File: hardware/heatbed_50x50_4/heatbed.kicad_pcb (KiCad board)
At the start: 2 copper layers, 50 x 50 mm, 1 part, among them J1 PWR

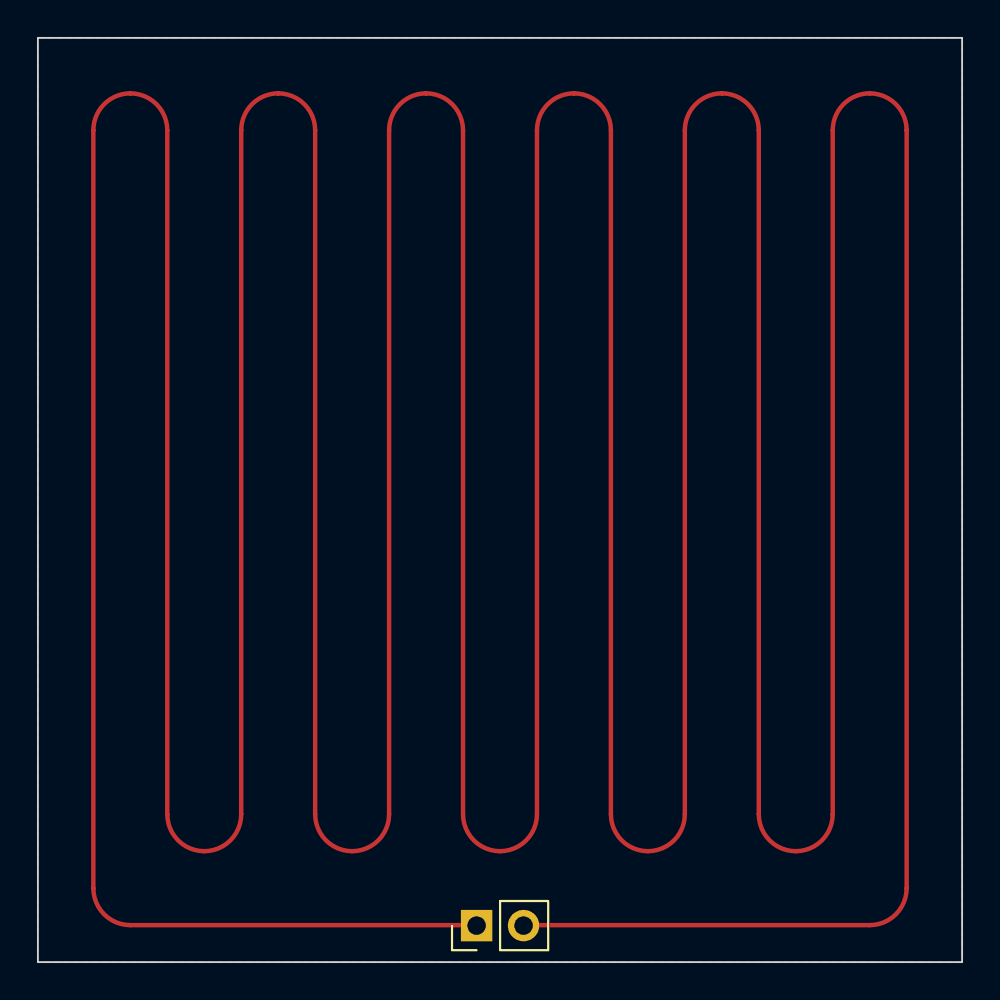
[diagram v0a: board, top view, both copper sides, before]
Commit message: Further increase tracks' widths
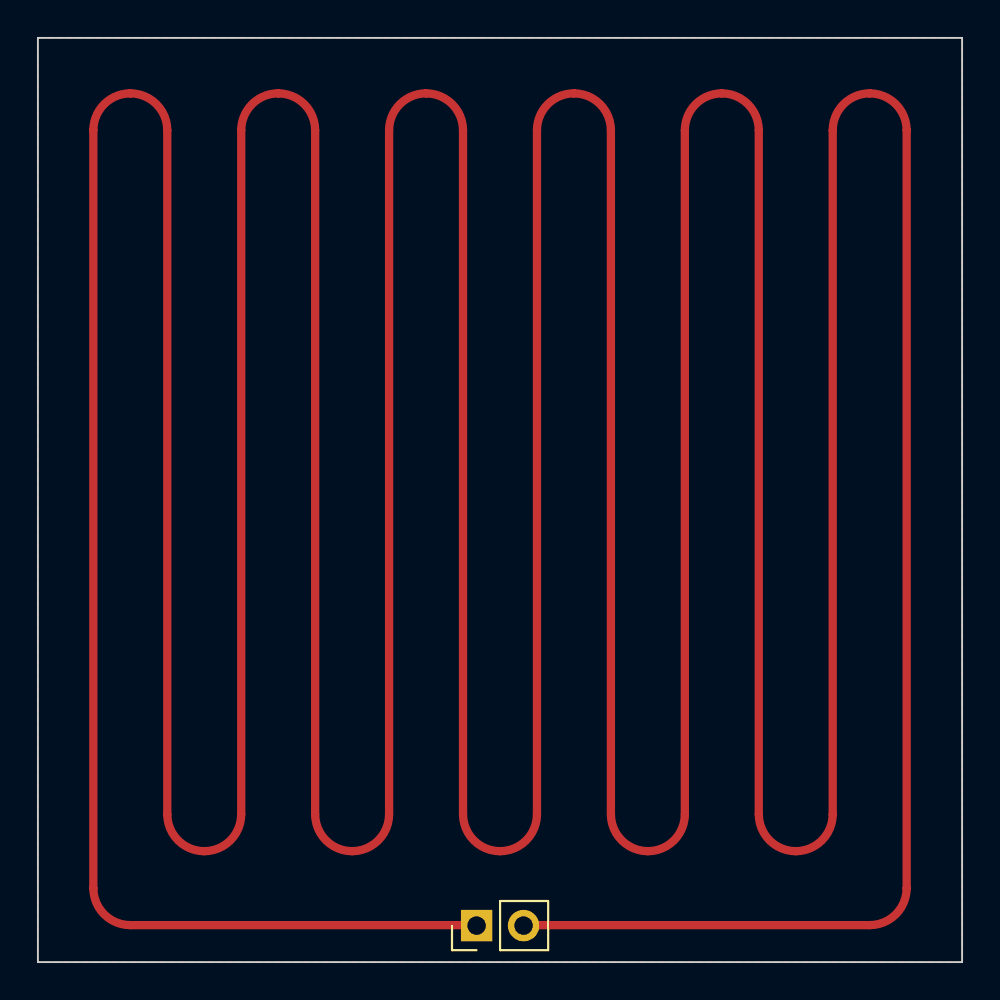
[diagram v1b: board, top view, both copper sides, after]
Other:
- board text added: "Width: 0.449 mm | Length: 564.93 mm | Resistance: 1.09 Ω"
- board text removed: "Width: 0.241 mm | Length: 564.93 mm | Resistance: 3.37 Ω"

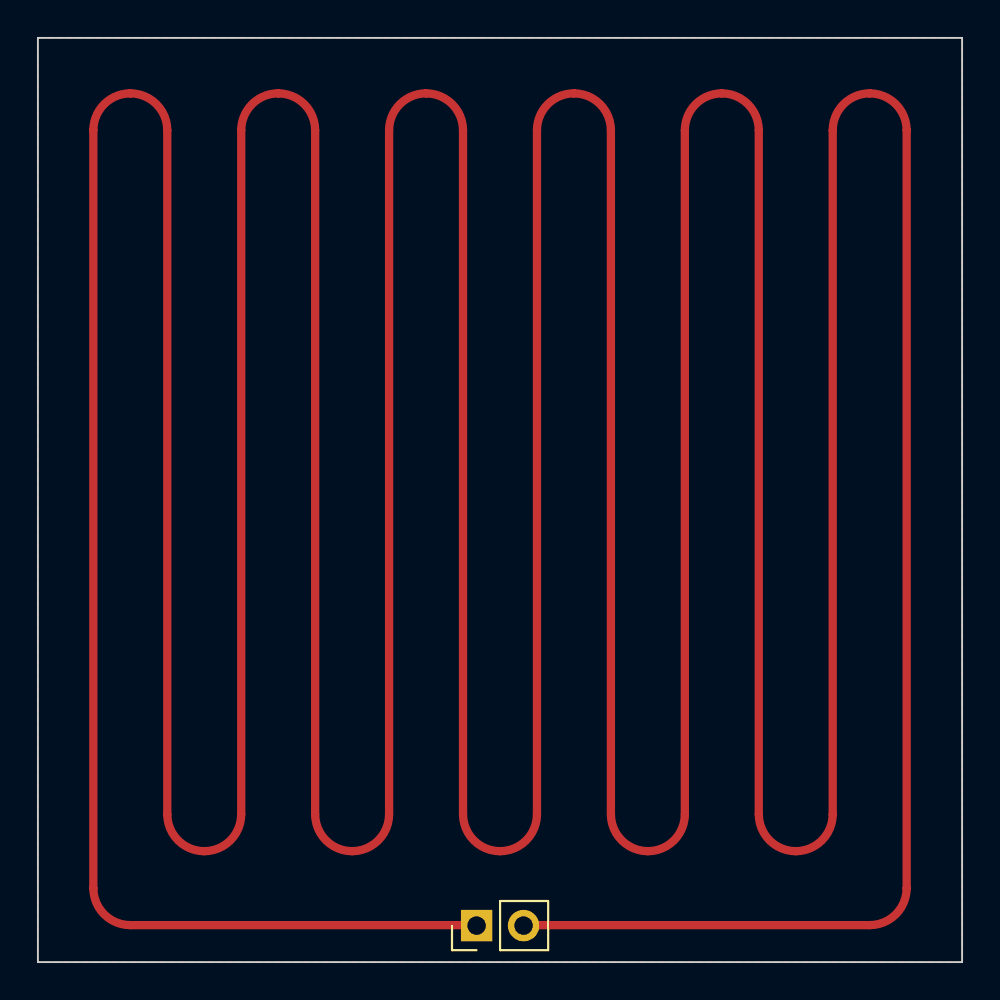
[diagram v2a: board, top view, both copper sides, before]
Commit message: Increase holes' diameters
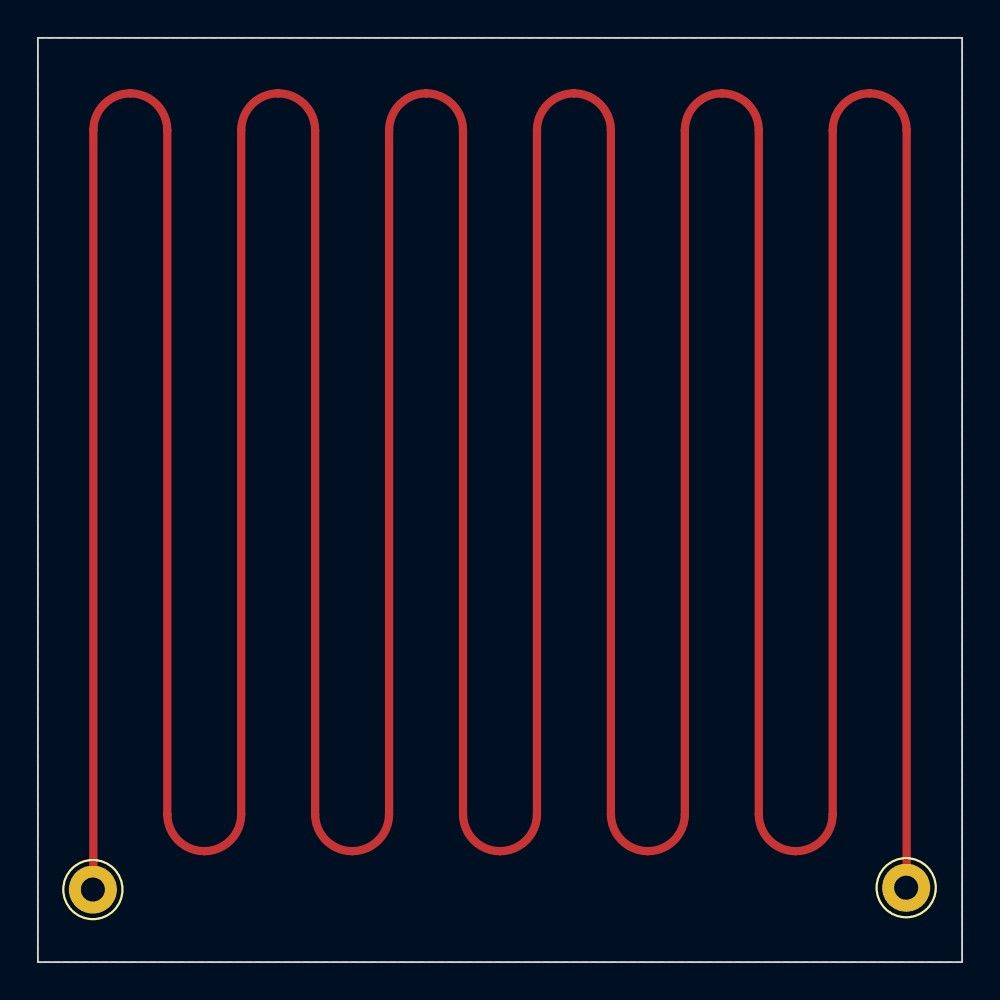
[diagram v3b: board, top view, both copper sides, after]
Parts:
- added J2: Conn_01x01, Connector_Pin:Pin_D1.3mm_L11.0mm, F.Cu at (168.0, 125.0)
- J1: value PWR -> Conn_01x01; footprint Connector_PinHeader_2.54mm:PinHeader_1x02_P2.54mm_Vertical -> Connector_Pin:Pin_D1.3mm_L11.0mm
- moved J1 20.9 mm to (124.0, 125.1), turned to 0 degrees
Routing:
- net Net-(J1-Pin_1): track 563.0 -> 519.4 mm
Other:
- board text removed: "Width: 0.449 mm | Length: 564.93 mm | Resistance: 1.09 Ω"
